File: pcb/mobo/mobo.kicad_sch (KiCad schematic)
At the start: 68 parts, among them J1 SWD_10, J2 PEEL_MOTOR, J3 DRIVE_MOTOR, J4 SW1, J5 SPRING_FINGERS, J6 SW2, J7 SW1, J8 USART1, J9 SWD_10, U1 STM32F031C6Tx, U2 STM32F031K6Ux, U4 AP1117-33, U5 MC34063AD, U6 MAX3078E, U7 DRV8837, U8 DRV8837, Y1 8MHz

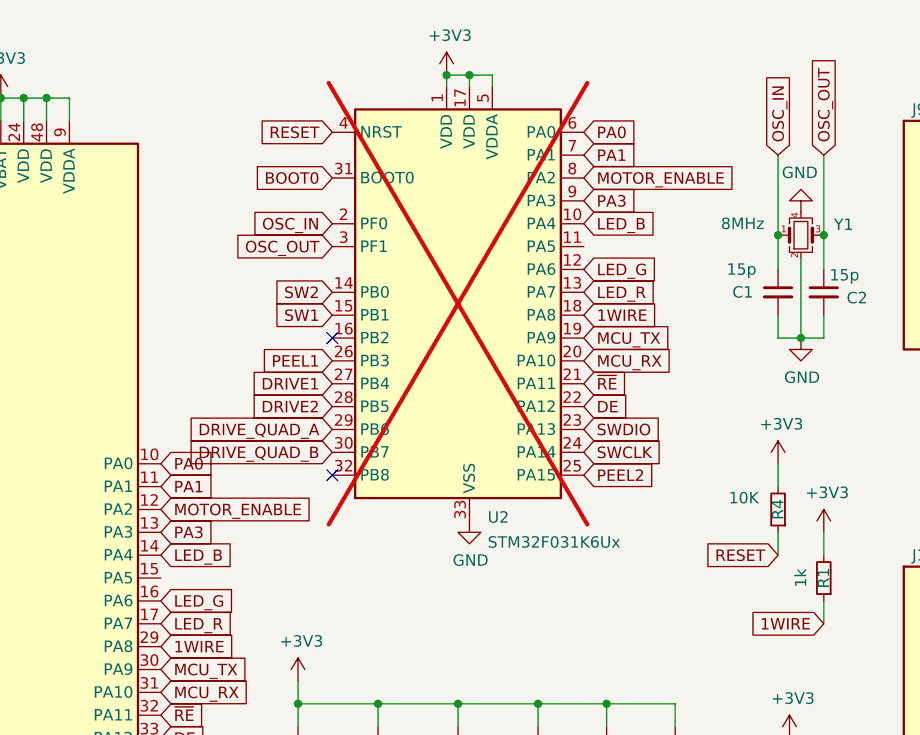
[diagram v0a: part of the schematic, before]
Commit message: Add REV12CD U1-only motherboard and three-board panel
Remove alternate U2 and its unused trace branches, retain U1 wiring, and label the derivative REV12CD. Add an editable routed three-up KiCad panel, shared PCB/stencil upload ZIP, assembly coordinates, reproducible export tools and validation reports.
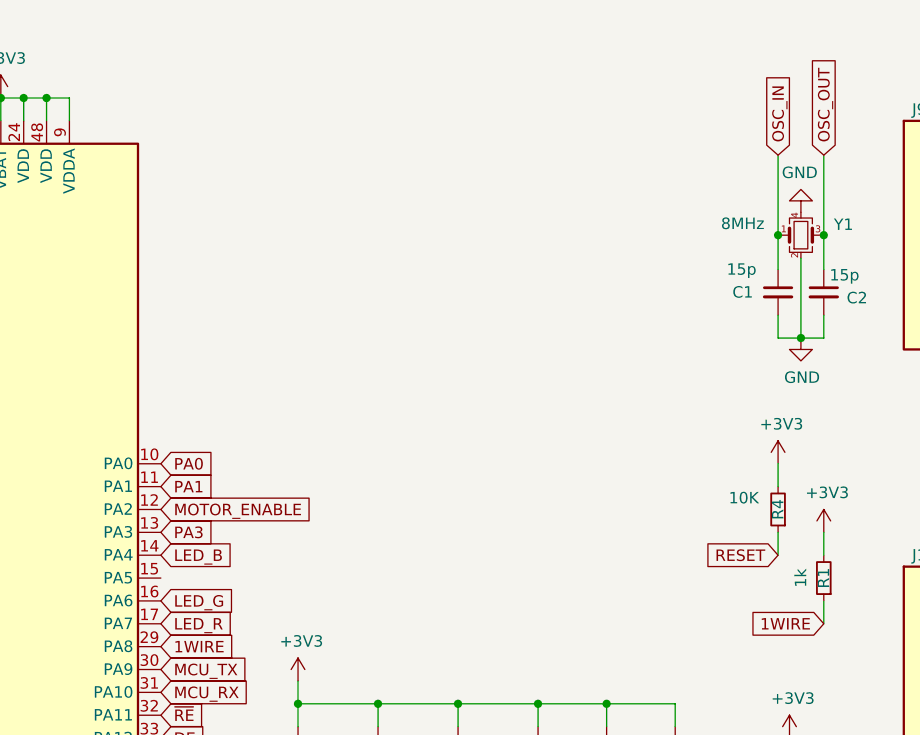
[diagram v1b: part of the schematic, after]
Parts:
- removed U2: STM32F031K6Ux, Package_DFN_QFN:QFN-32-1EP_5x5mm_P0.5mm_EP3.45x3.45mm, symbol MCU_ST_STM32F0:STM32F031K6Ux
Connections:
- no-connect marks 8 -> 6
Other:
- company: Opulo, Inc. -> crazydart; derived from Opulo REV12
- title: LumenPnP Feeder Control Board -> Feeder motherboard - U1 only
